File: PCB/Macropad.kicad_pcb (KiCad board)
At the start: 2 copper layers, 24 parts, among them SW1 SW_Push, U1 ATmega32U4-AU, Y1 16MHz

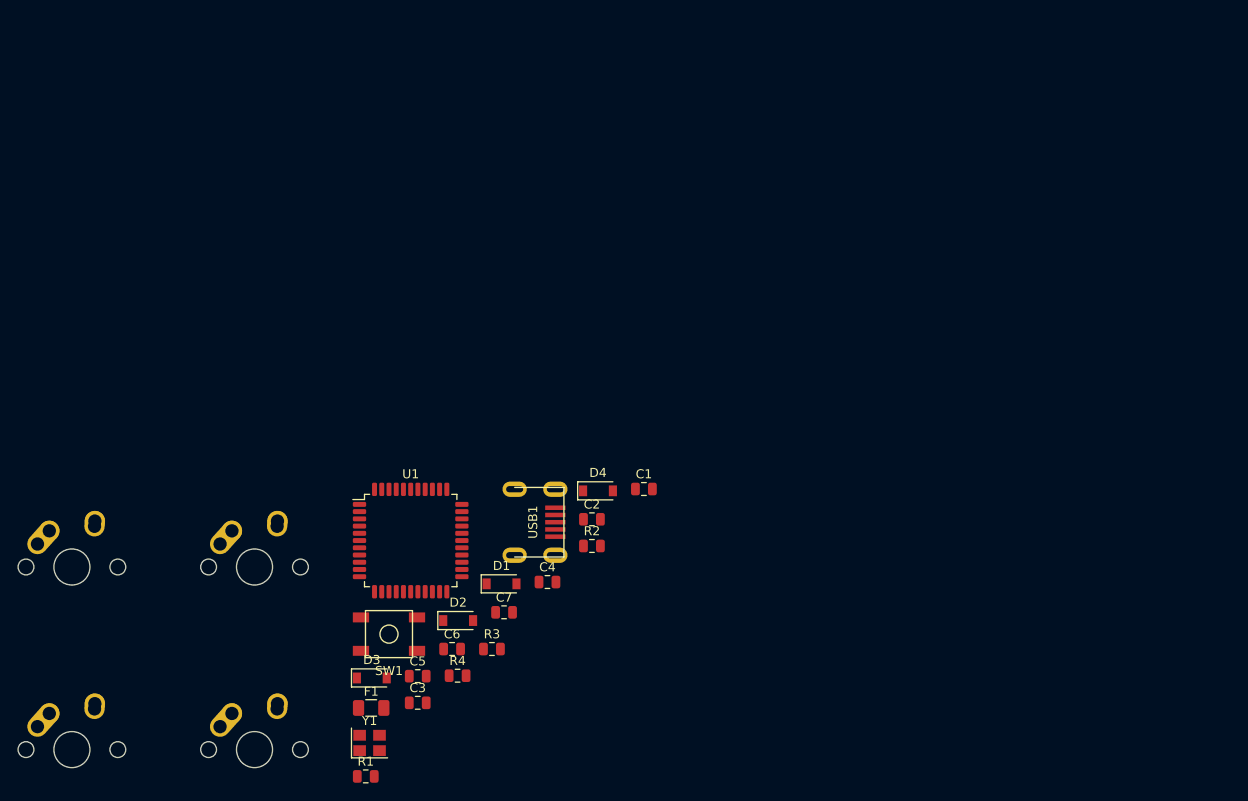
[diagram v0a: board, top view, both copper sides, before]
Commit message: Components Placed, Routing to be done
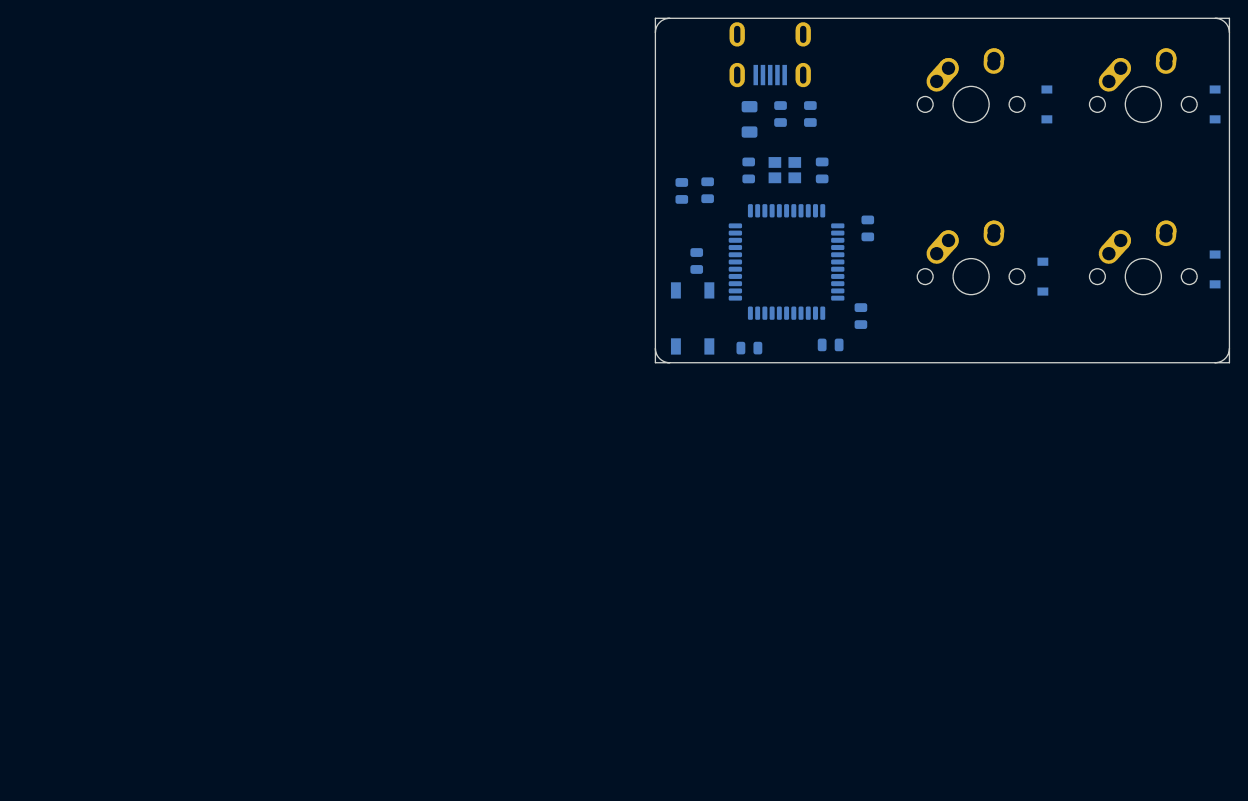
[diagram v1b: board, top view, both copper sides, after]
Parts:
- C1, C2, C3, C4, C5, C6, C7, D1, D2, D3, D4, F1, R1, R2, R3, R4, SW1, U1, USB1, Y1: moved to B.Cu
- moved MX2 138.3 mm to (149.2, 41.3)
- moved MX1 111.9 mm to (130.2, 41.3)
- moved MX4 103.4 mm to (149.2, 60.3)
- moved D2 101.3 mm to (157.2, 41.3), turned to 90 degrees
- moved MX3 95.0 mm to (130.2, 60.3)
- moved D3 86.5 mm to (138.1, 60.3), turned to 90 degrees
- moved D1 80.3 mm to (138.6, 41.3), turned to 90 degrees
- moved Y1 78.3 mm to (109.6, 48.5)
- moved F1 77.4 mm to (105.7, 42.9), turned to 90 degrees
- moved R1 73.6 mm to (98.2, 50.8), turned to 90 degrees
- moved D4 72.5 mm to (157.2, 59.5), turned to 90 degrees
- moved R3 67.2 mm to (109.1, 42.3), turned to 90 degrees
- moved C5 62.6 mm to (101.0, 50.8), turned to 90 degrees
- moved USB1 60.9 mm to (108.0, 33.5), turned to 270 degrees
- moved R4 59.8 mm to (118.0, 64.7), turned to 90 degrees
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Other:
- board outline added: 63.5 x 38.1 mm
